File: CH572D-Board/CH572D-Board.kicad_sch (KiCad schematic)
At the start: 17 parts, among them J1 12402012E212A, J2 Conn_PinHeader_1x07_P2.54mm_V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, U2 the really cheap one (200mah), Y1 32mhz

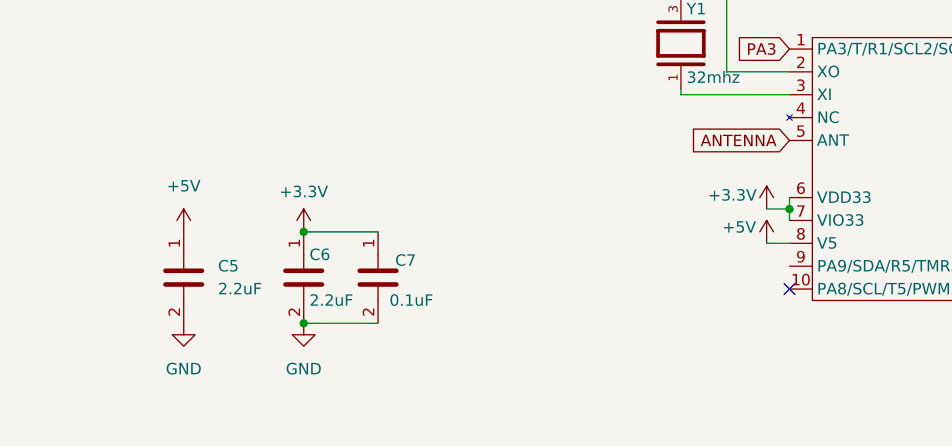
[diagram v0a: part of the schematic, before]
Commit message: starting work on the board mk2, stripping all components off I can
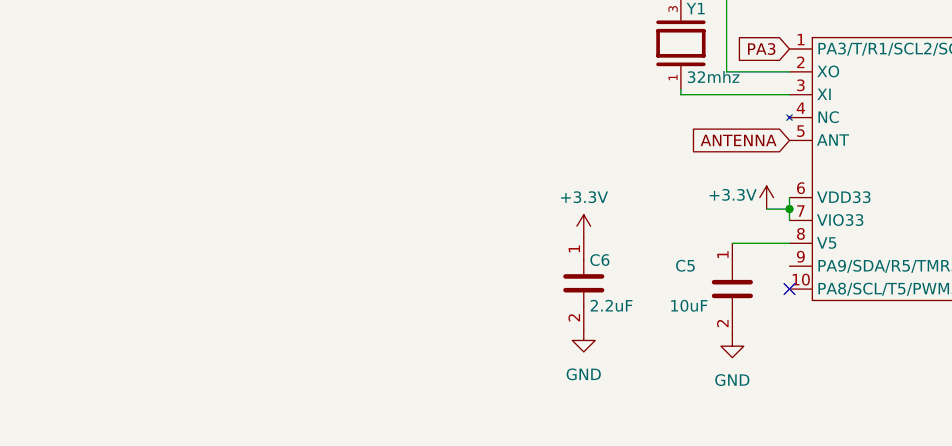
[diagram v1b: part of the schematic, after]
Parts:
- removed C7: 0.1uF, Personal:0603, symbol 0603:C_0603
- C5: value 2.2uF -> 10uF
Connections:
- net +5V: no longer C5.1, U1.8 (V5)
- new net: C5.1, U1.8 (V5)
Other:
- moved on the sheet: C5, C6
